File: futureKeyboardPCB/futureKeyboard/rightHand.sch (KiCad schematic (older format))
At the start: 50 parts

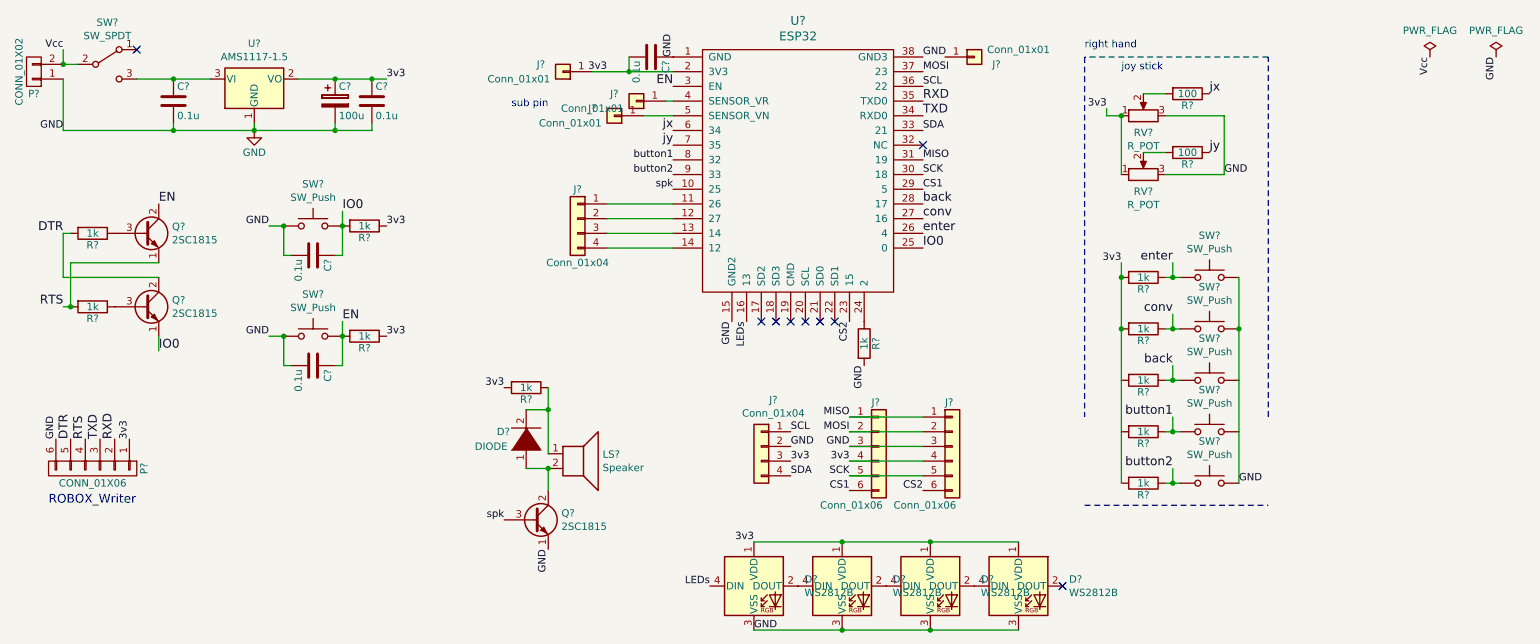
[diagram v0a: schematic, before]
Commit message: add left hand circuit on .sch file
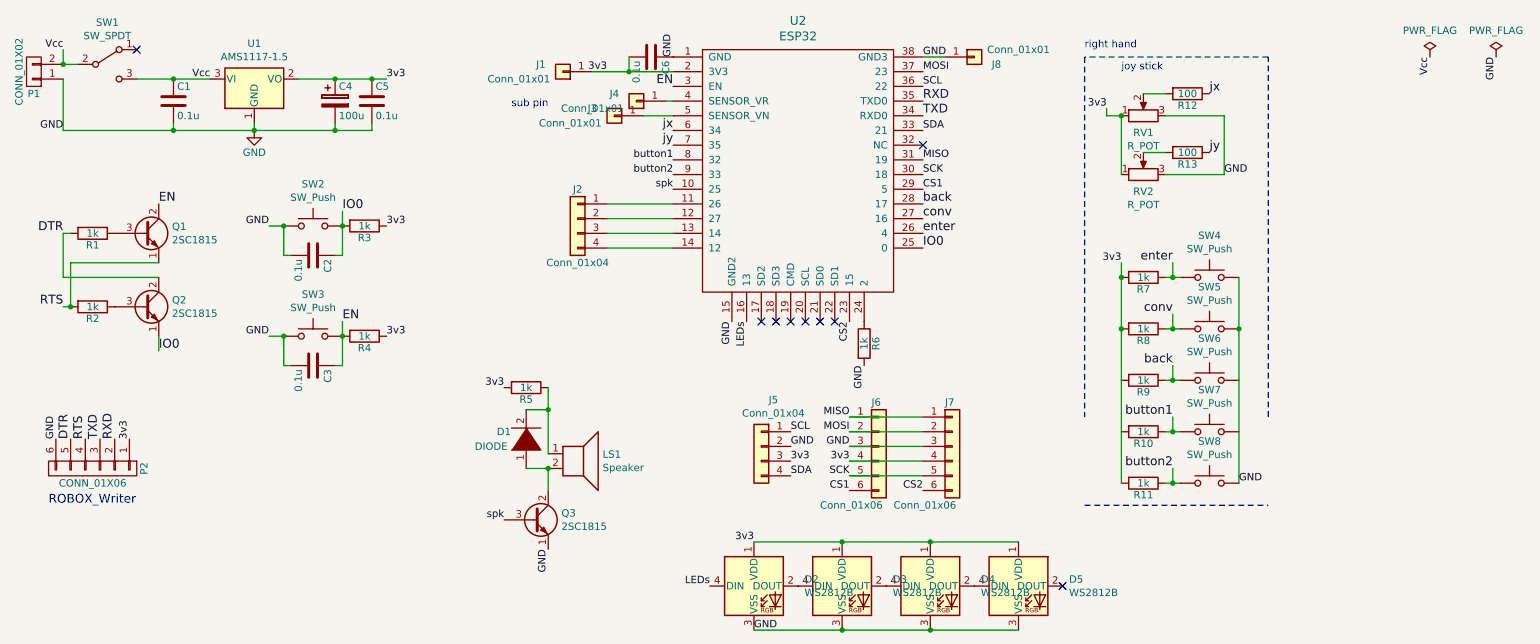
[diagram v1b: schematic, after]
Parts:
- gave numbers to parts that had none: 50
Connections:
- net GND: now also J8.1 (Pin_1)
- net Vcc: now also C1.1, SW1.3 (C), U1.3 (VI)

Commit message: create net list
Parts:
- C1, C2, C3, C5, C6: footprint akizukit:SMD-2012 -> akizukit:SMD-1608
- D1: footprint (none) -> Diode_THT:D_A-405_P7.62mm_Horizontal
- J1, J3, J4, J8: footprint (none) -> Connector_PinHeader_2.54mm:PinHeader_1x01_P2.54mm_Vertical
- J2, J5: footprint (none) -> Connector_PinHeader_2.54mm:PinHeader_1x04_P2.54mm_Vertical
- J6, J7: footprint (none) -> Connector_PinHeader_2.54mm:PinHeader_1x06_P2.54mm_Vertical
- LS1: footprint (none) -> akizukit:small_speaker
- SW4, SW5, SW6: footprint akizukit:SMD_SW -> Button_Switch_Keyboard:SW_Cherry_MX_1.00u_PCB
- U1: footprint Package_TO_SOT_SMD:SOT-223-3_TabPin2 -> akizukit:AZ1086H
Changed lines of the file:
@@
 F 0 "SW4" H 8900 2735 50  0000 C CNN
 F 1 "SW_Push" H 8900 2644 50  0000 C CNN
-F 2 "akizukit:SMD_SW" H 8900 2650 50  0001 C CNN
+F 2 "Button_Switch_Keyboard:SW_Cherry_MX_1.00u_PCB" H 8900 2650 50  0001 C CNN
 F 3 "~" H 8900 2650 50  0001 C CNN
 	1    8900 2450
@@
 F 0 "SW5" H 8900 3085 50  0000 C CNN
 F 1 "SW_Push" H 8900 2994 50  0000 C CNN
-F 2 "akizukit:SMD_SW" H 8900 3000 50  0001 C CNN
+F 2 "Button_Switch_Keyboard:SW_Cherry_MX_1.00u_PCB" H 8900 3000 50  0001 C CNN
 F 3 "~" H 8900 3000 50  0001 C CNN
 	1    8900 2800
@@
 F 0 "SW6" H 8900 3435 50  0000 C CNN
 F 1 "SW_Push" H 8900 3344 50  0000 C CNN
-F 2 "akizukit:SMD_SW" H 8900 3350 50  0001 C CNN
+F 2 "Button_Switch_Keyboard:SW_Cherry_MX_1.00u_PCB" H 8900 3350 50  0001 C CNN
 F 3 "~" H 8900 3350 50  0001 C CNN
 	1    8900 3150
@@
 F 0 "C1" H 1875 1350 50  0000 L CNN
 F 1 "0.1u" H 1875 1150 50  0000 L CNN
-F 2 "akizukit:SMD-2012" H 1888 1100 50  0001 C CNN
+F 2 "akizukit:SMD-1608" H 1888 1100 50  0001 C CNN
 F 3 "" H 1850 1250 50  0000 C CNN
 	1    1850 1250
@@
 F 0 "C5" H 3225 1350 50  0000 L CNN
 F 1 "0.1u" H 3225 1150 50  0000 L CNN
-F 2 "akizukit:SMD-2012" H 3238 1100 50  0001 C CNN
+F 2 "akizukit:SMD-1608" H 3238 1100 50  0001 C CNN
 F 3 "" H 3200 1250 50  0000 C CNN
 	1    3200 1250
@@
 F 0 "C6" H 5125 1050 50  0000 L CNN
 F 1 "0.1u" H 5125 850 50  0000 L CNN
-F 2 "akizukit:SMD-2012" H 5138 800 50  0001 C CNN
+F 2 "akizukit:SMD-1608" H 5138 800 50  0001 C CNN
 F 3 "" H 5100 950 50  0000 C CNN
 	1    5100 950
@@
 F 0 "C2" H 2825 2400 50  0000 L CNN
 F 1 "0.1u" H 2825 2200 50  0000 L CNN
-F 2 "akizukit:SMD-2012" H 2838 2150 50  0001 C CNN
+F 2 "akizukit:SMD-1608" H 2838 2150 50  0001 C CNN
 F 3 "" H 2800 2300 50  0000 C CNN
 	1    2800 2300
@@
 F 0 "C3" H 2825 3150 50  0000 L CNN
 F 1 "0.1u" H 2825 2950 50  0000 L CNN
-F 2 "akizukit:SMD-2012" H 2838 2900 50  0001 C CNN
+F 2 "akizukit:SMD-1608" H 2838 2900 50  0001 C CNN
 F 3 "" H 2800 3050 50  0000 C CNN
 	1    2800 3050
@@
 F 0 "U1" H 2400 1342 50  0000 C CNN
 F 1 "AMS1117-1.5" H 2400 1251 50  0000 C CNN
-F 2 "Package_TO_SOT_SMD:SOT-223-3_TabPin2" H 2400 1300 50  0001 C CNN
+F 2 "akizukit:AZ1086H" H 2400 1300 50  0001 C CNN
 F 3 "http://www.advanced-monolithic.com/pdf/ds1117.pdf" H 2500 850 50  0001 C CNN
 	1    2400 1100
@@
 F 0 "LS1" H 4770 3646 50  0000 L CNN
 F 1 "Speaker" H 4770 3555 50  0000 L CNN
-F 2 "" H 4600 3450 50  0001 C CNN
+F 2 "akizukit:small_speaker" H 4600 3450 50  0001 C CNN
 F 3 "~" H 4590 3600 50  0001 C CNN
 	1    4600 3650
@@
 F 0 "D1" V 4300 3750 50  0000 R CNN
 F 1 "DIODE" V 4200 3900 50  0000 R CNN
-F 2 "" H 4250 3550 50  0001 C CNN
+F 2 "Diode_THT:D_A-405_P7.62mm_Horizontal" H 4250 3550 50  0001 C CNN
 F 3 "~" H 4250 3550 50  0001 C CNN
 	1    4250 3550
@@
 F 0 "J4" H 5150 1200 50  0000 C CNN
 F 1 "Conn_01x01" H 5300 1300 50  0000 C CNN
-F 2 "" H 5000 1250 50  0001 C CNN
+F 2 "Connector_PinHeader_2.54mm:PinHeader_1x01_P2.54mm_Vertical" H 5000 1250 50  0001 C CNN
 F 3 "~" H 5000 1250 50  0001 C CNN
 	1    5000 1250
@@
 F 0 "J1" H 4650 1000 50  0000 C CNN
 F 1 "Conn_01x01" H 4800 1100 50  0000 C CNN
-F 2 "" H 4500 1050 50  0001 C CNN
+F 2 "Connector_PinHeader_2.54mm:PinHeader_1x01_P2.54mm_Vertical" H 4500 1050 50  0001 C CNN
 F 3 "~" H 4500 1050 50  0001 C CNN
 	1    4500 1050
@@
 F 0 "J8" H 7450 900 50  0000 C CNN
 F 1 "Conn_01x01" H 7600 1000 50  0000 C CNN
-F 2 "" H 7300 950 50  0001 C CNN
+F 2 "Connector_PinHeader_2.54mm:PinHeader_1x01_P2.54mm_Vertical" H 7300 950 50  0001 C CNN
 F 3 "~" H 7300 950 50  0001 C CNN
 	1    7300 950
@@
 F 0 "J3" H 5000 1300 50  0000 C CNN
 F 1 "Conn_01x01" H 5150 1400 50  0000 C CNN
-F 2 "" H 4850 1350 50  0001 C CNN
+F 2 "Connector_PinHeader_2.54mm:PinHeader_1x01_P2.54mm_Vertical" H 4850 1350 50  0001 C CNN
 F 3 "~" H 4850 1350 50  0001 C CNN
 	1    4850 1350
@@
 F 0 "J6" H 6600 3900 50  0000 L CNN
 F 1 "Conn_01x06" H 6250 3200 50  0000 L CNN
-F 2 "" H 6650 3600 50  0001 C CNN
+F 2 "Connector_PinHeader_2.54mm:PinHeader_1x06_P2.54mm_Vertical" H 6650 3600 50  0001 C CNN
 F 3 "~" H 6650 3600 50  0001 C CNN
 	1    6650 3600
@@
 F 0 "J7" H 7100 3900 50  0000 L CNN
 F 1 "Conn_01x06" H 6750 3200 50  0000 L CNN
-F 2 "" H 7150 3600 50  0001 C CNN
+F 2 "Connector_PinHeader_2.54mm:PinHeader_1x06_P2.54mm_Vertical" H 7150 3600 50  0001 C CNN
 F 3 "~" H 7150 3600 50  0001 C CNN
 	1    7150 3600
@@
 F 0 "J5" H 5768 3917 50  0000 C CNN
 F 1 "Conn_01x04" H 5768 3826 50  0000 C CNN
-F 2 "" H 5850 3600 50  0001 C CNN
+F 2 "Connector_PinHeader_2.54mm:PinHeader_1x04_P2.54mm_Vertical" H 5850 3600 50  0001 C CNN
 F 3 "~" H 5850 3600 50  0001 C CNN
 	1    5850 3600
@@
 F 0 "J2" H 4600 2250 50  0000 C CNN
 F 1 "Conn_01x04" H 4600 1750 50  0000 C CNN
-F 2 "" H 4600 2050 50  0001 C CNN
+F 2 "Connector_PinHeader_2.54mm:PinHeader_1x04_P2.54mm_Vertical" H 4600 2050 50  0001 C CNN
 F 3 "~" H 4600 2050 50  0001 C CNN
 	1    4600 2050
